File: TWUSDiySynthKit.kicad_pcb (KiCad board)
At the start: 2 copper layers, 198.4 x 65 mm, 58 parts, among them J1 Conn_02x02_Counter_Clockwise, J10 Conn_01x03_Socket, J11 Conn_01x03_Socket, J12 Conn_01x03_Socket, J14 Conn_01x04_Socket, J2 Conn_01x02, J3 Conn_01x07_Pin, J4 Conn_01x07_Pin, J5 Raspberry_Pi_2x20_PTH, J6 Conn_01x04_Socket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

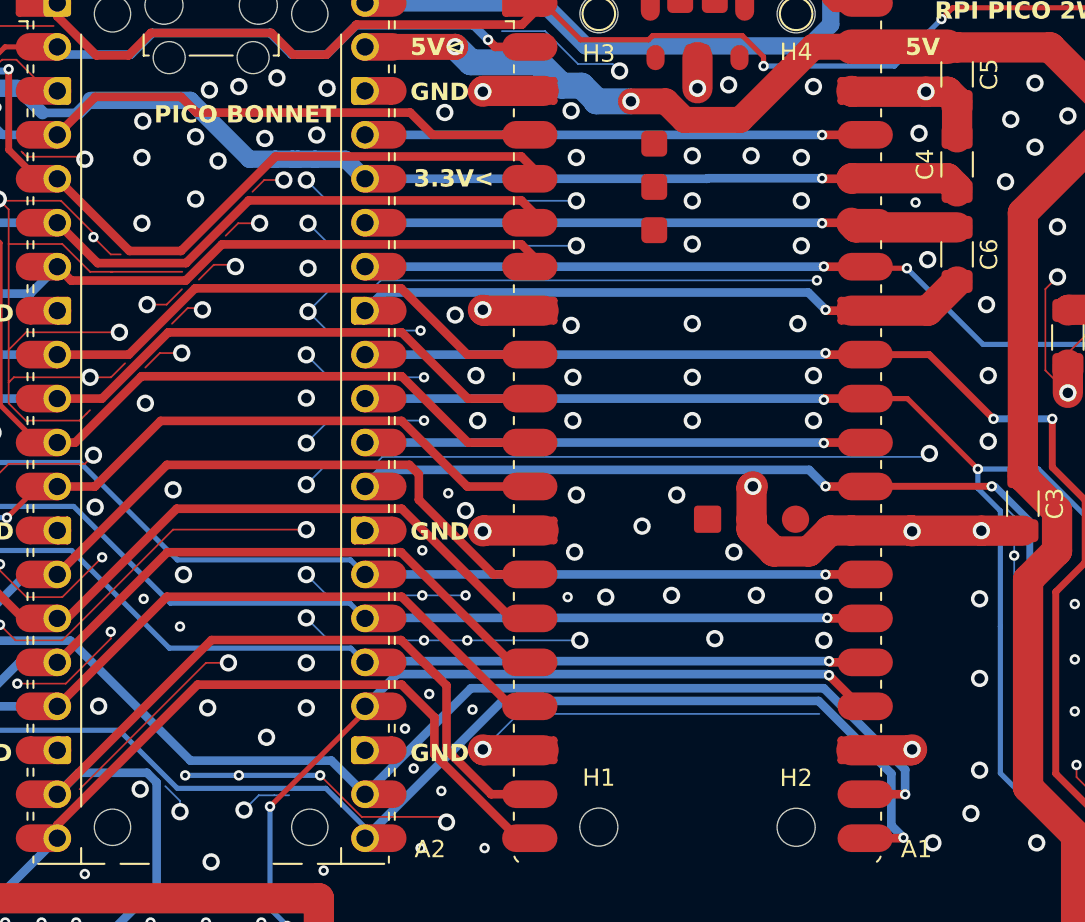
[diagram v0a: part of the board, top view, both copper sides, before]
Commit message: Improve ground stitching
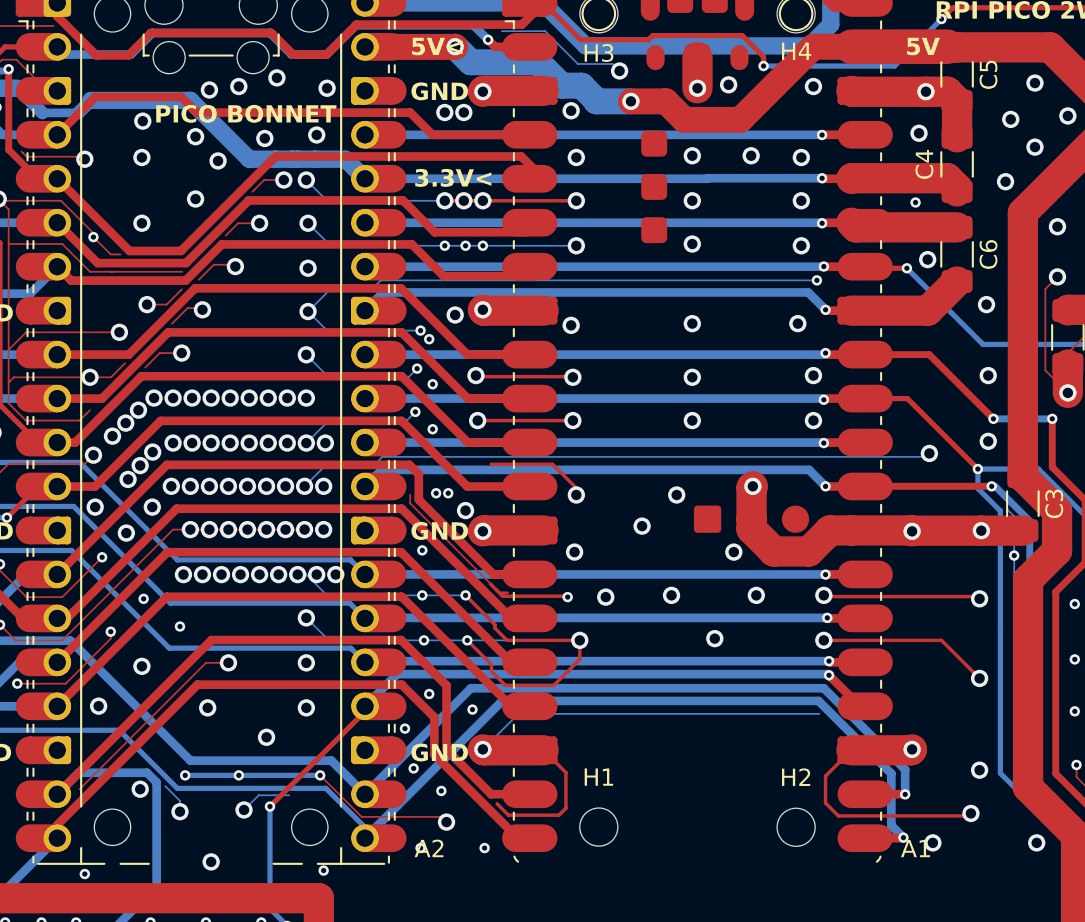
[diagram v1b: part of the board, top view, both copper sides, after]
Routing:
- net GND: track 1284.8 -> 1380.8 mm, vias 813 -> 869
- net Net-(A1-GPIO4): track 44.7 -> 43.9 mm

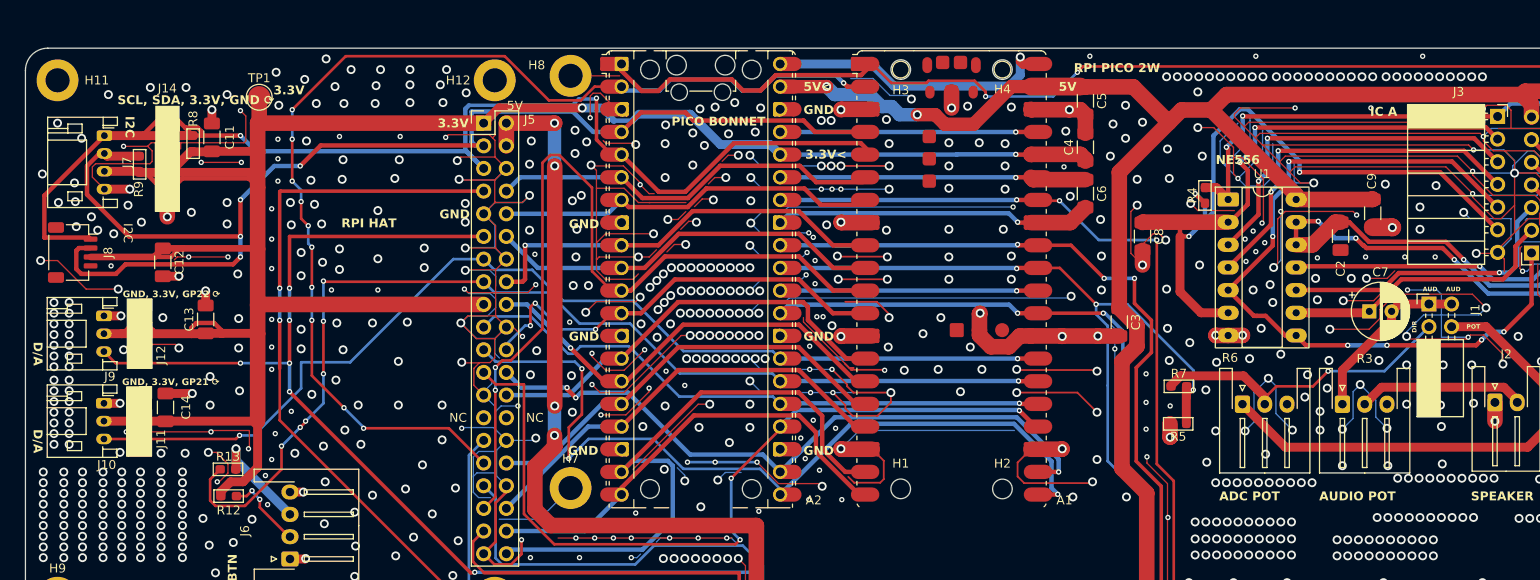
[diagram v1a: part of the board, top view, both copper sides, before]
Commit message: Added bill of materials
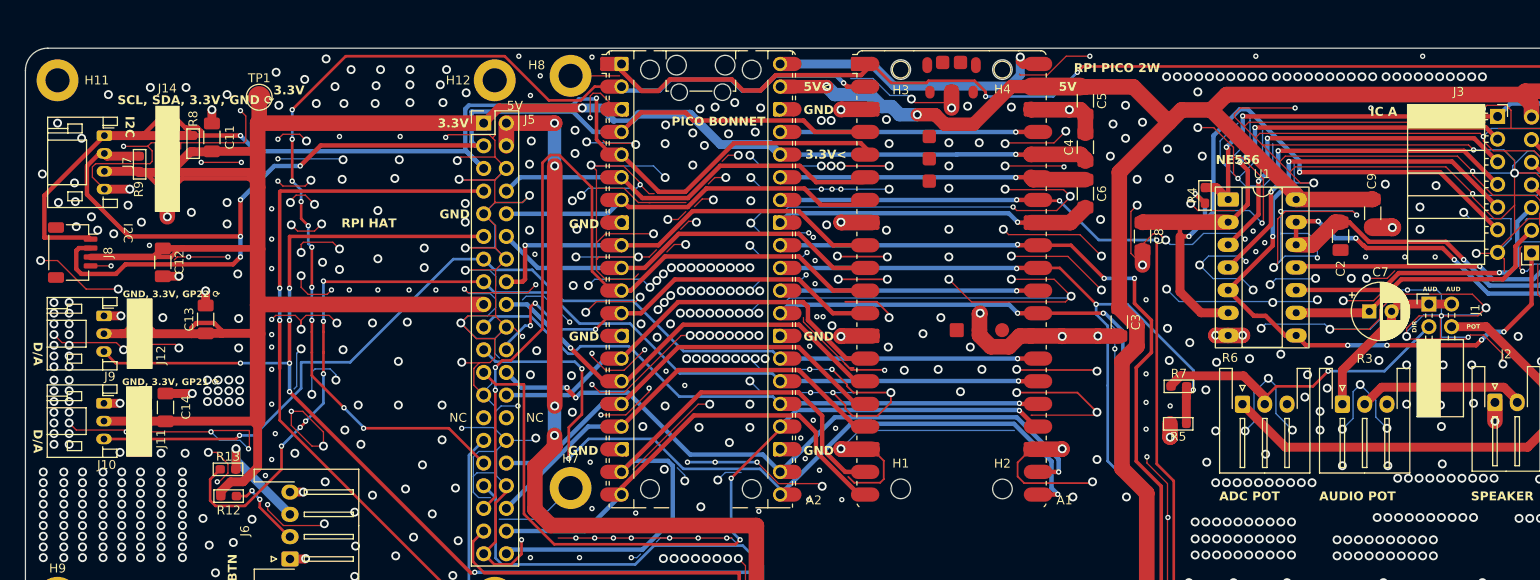
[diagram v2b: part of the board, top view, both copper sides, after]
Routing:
- net GND: track 1380.8 -> 1722.6 mm, vias 869 -> 892

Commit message: Added logo
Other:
- board text added: "Designed by GreeniusGenius™"

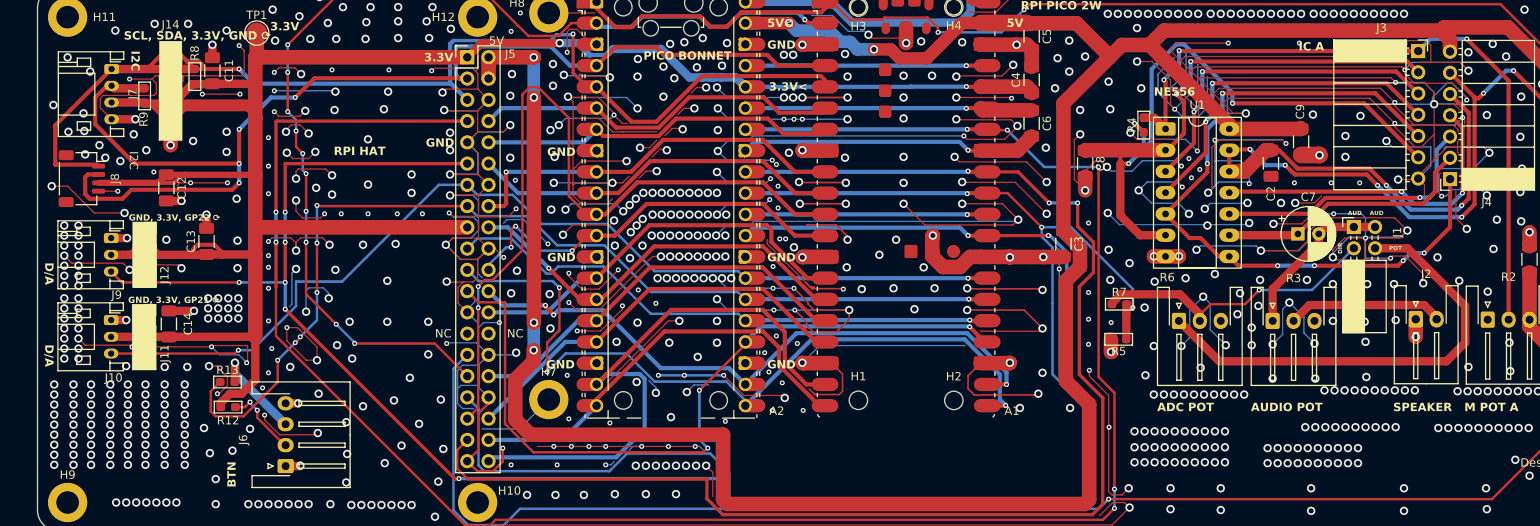
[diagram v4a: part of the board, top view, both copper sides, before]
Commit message: widened gnd traces and connected missing gpio trace
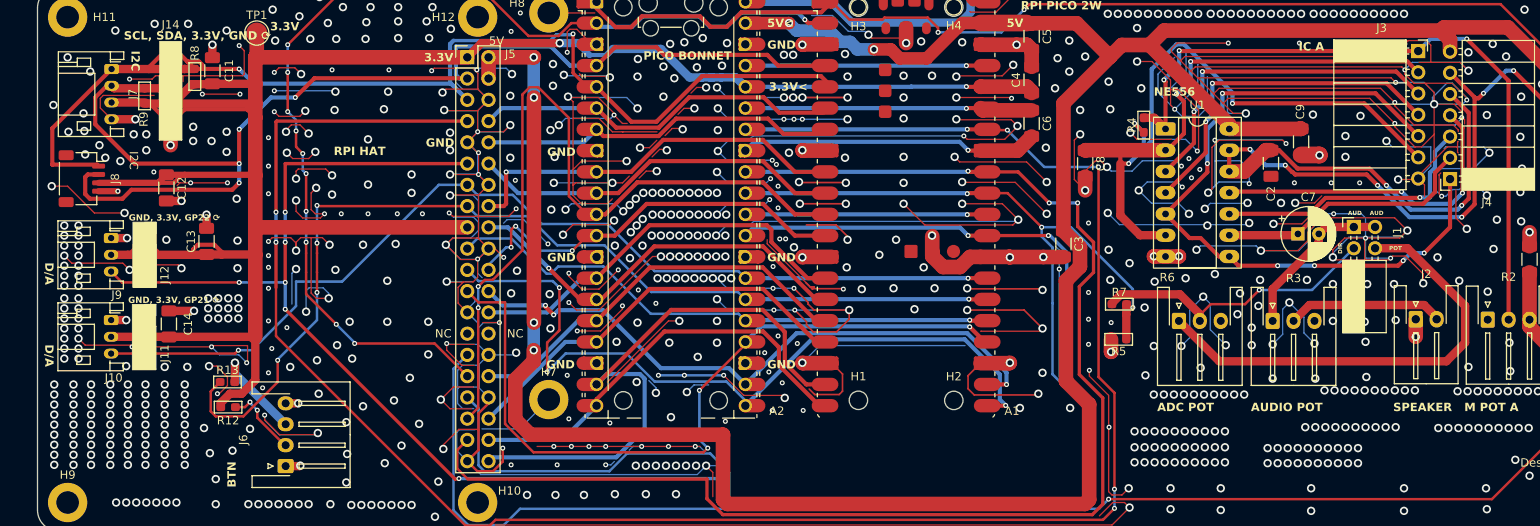
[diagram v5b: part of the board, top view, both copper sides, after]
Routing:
- net GND: track 1722.6 -> 1817.5 mm, vias 892 -> 900
- net Net-(A1-GPIO2): track 141.0 -> 144.2 mm
- net Net-(A1-GPIO3): track 136.7 -> 137.2 mm
- net Net-(A1-GPIO20): vias 7 -> 5
